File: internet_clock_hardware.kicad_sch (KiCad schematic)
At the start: 10 parts, among them U1 MM5451

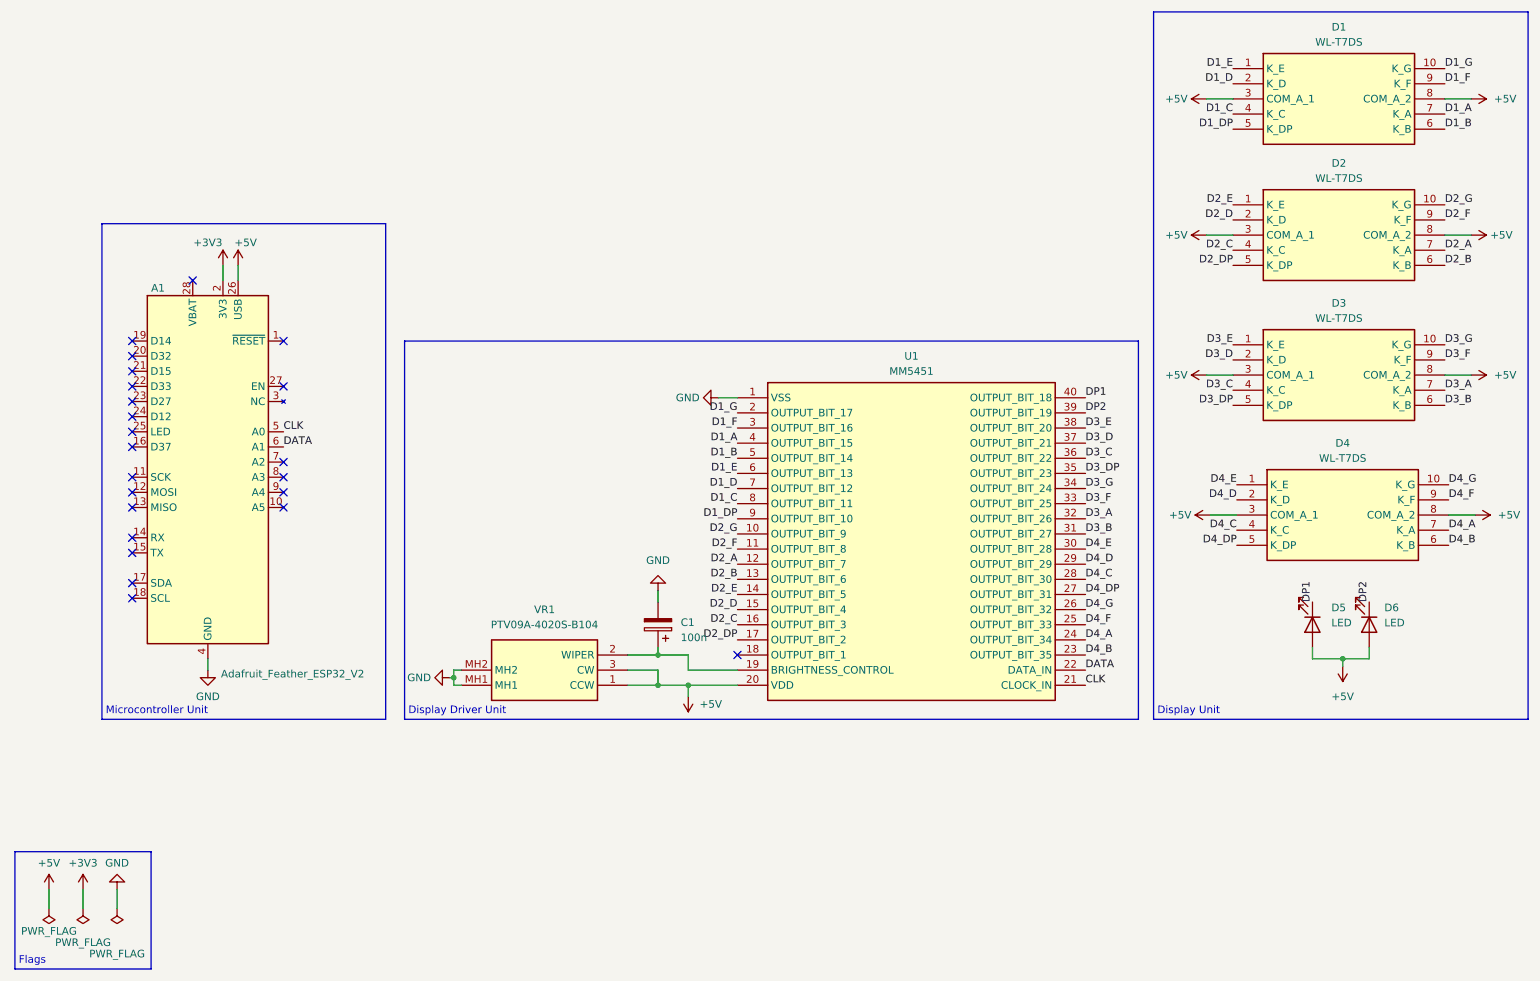
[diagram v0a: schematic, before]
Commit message: added 3d models
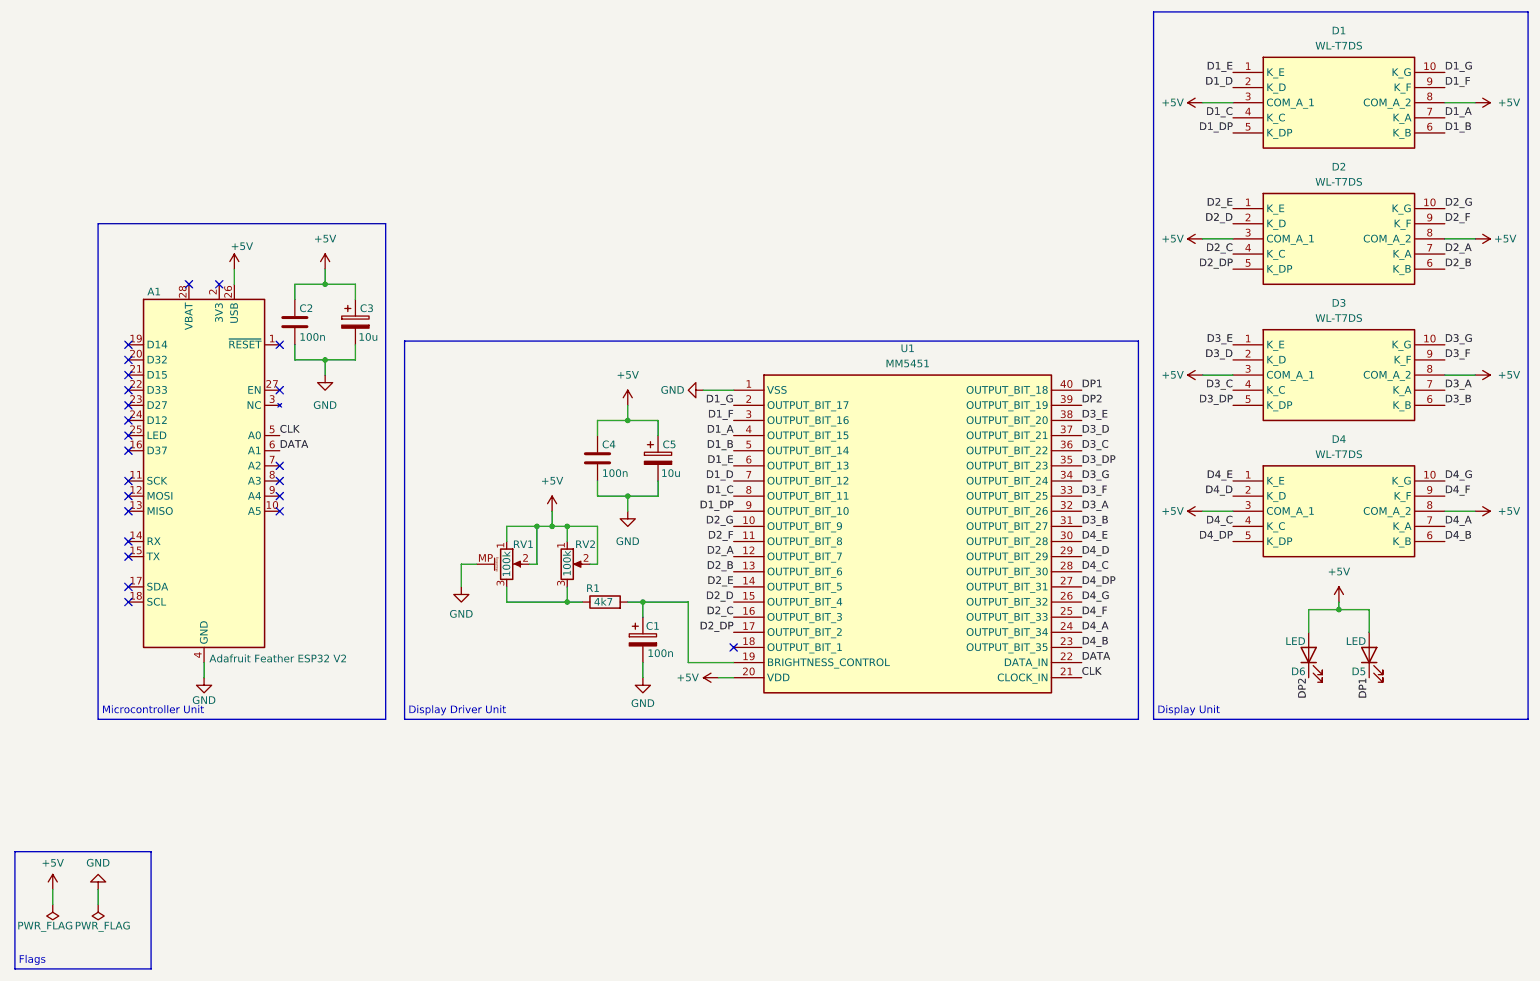
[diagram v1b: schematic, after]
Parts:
- removed VR1: PTV09A-4020S-B104, PTV09A-4020S-B104:PTV09A4020SB104, symbol PTV09A-4020S-B104:PTV09A-4020S-B104
- added C2, C4: 100n, Capacitor_THT:C_Rect_L4.6mm_W2.0mm_P2.50mm_MKS02_FKP02, symbol Device:C
- added C3, C5: 10u, Capacitor_THT:CP_Radial_D5.0mm_P2.00mm, symbol Device:C_Polarized
- added R1: 4k7, Resistor_THT:R_Axial_DIN0207_L6.3mm_D2.5mm_P10.16mm_Horizontal, symbol Device:R
- added RV1: 100k, PTV09A-4020S-B104:PTV09A4020SB104, symbol Device:R_Potentiometer_MountingPin
- added RV2: 100k, Potentiometer_THT:Potentiometer_Vishay_T73YP_Vertical, symbol Device:R_Potentiometer
- A1: value Adafruit_Feather_ESP32_V2 -> Adafruit Feather ESP32 V2
- C1: footprint Capacitor_THT:CP_Radial_D5.0mm_P2.00mm -> Capacitor_THT:C_Rect_L4.6mm_W2.0mm_P2.50mm_MKS02_FKP02
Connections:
- net +5V: now also C2.1, C3.1, C4.1, C5.1, RV1.1, RV1.2, RV2.1, RV2.2
- net GND: now also C2.2, C3.2, C4.2, C5.2, RV1.MP (MountPin)
- net at C1.1, U1.19 (BRIGHTNESS_CONTROL): now also R1.2
- net +3V3: no longer names the net of A1.2 (3V3)
- new net: R1.1, RV1.3, RV2.3
- no-connect marks 23 -> 24
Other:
- moved on the sheet: A1, C1, D1, D2, D4, D5, D6, U1
